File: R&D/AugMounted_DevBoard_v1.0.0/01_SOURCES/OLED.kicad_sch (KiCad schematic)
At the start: 30 parts, among them J3 J_FH43BW-61S-0.2SHW, Q1 Q_BSS123WQ-7-F, U4 U_TXB0108PWR, U5 U_TXB0108PWR, U6 U_TXB0108PWR

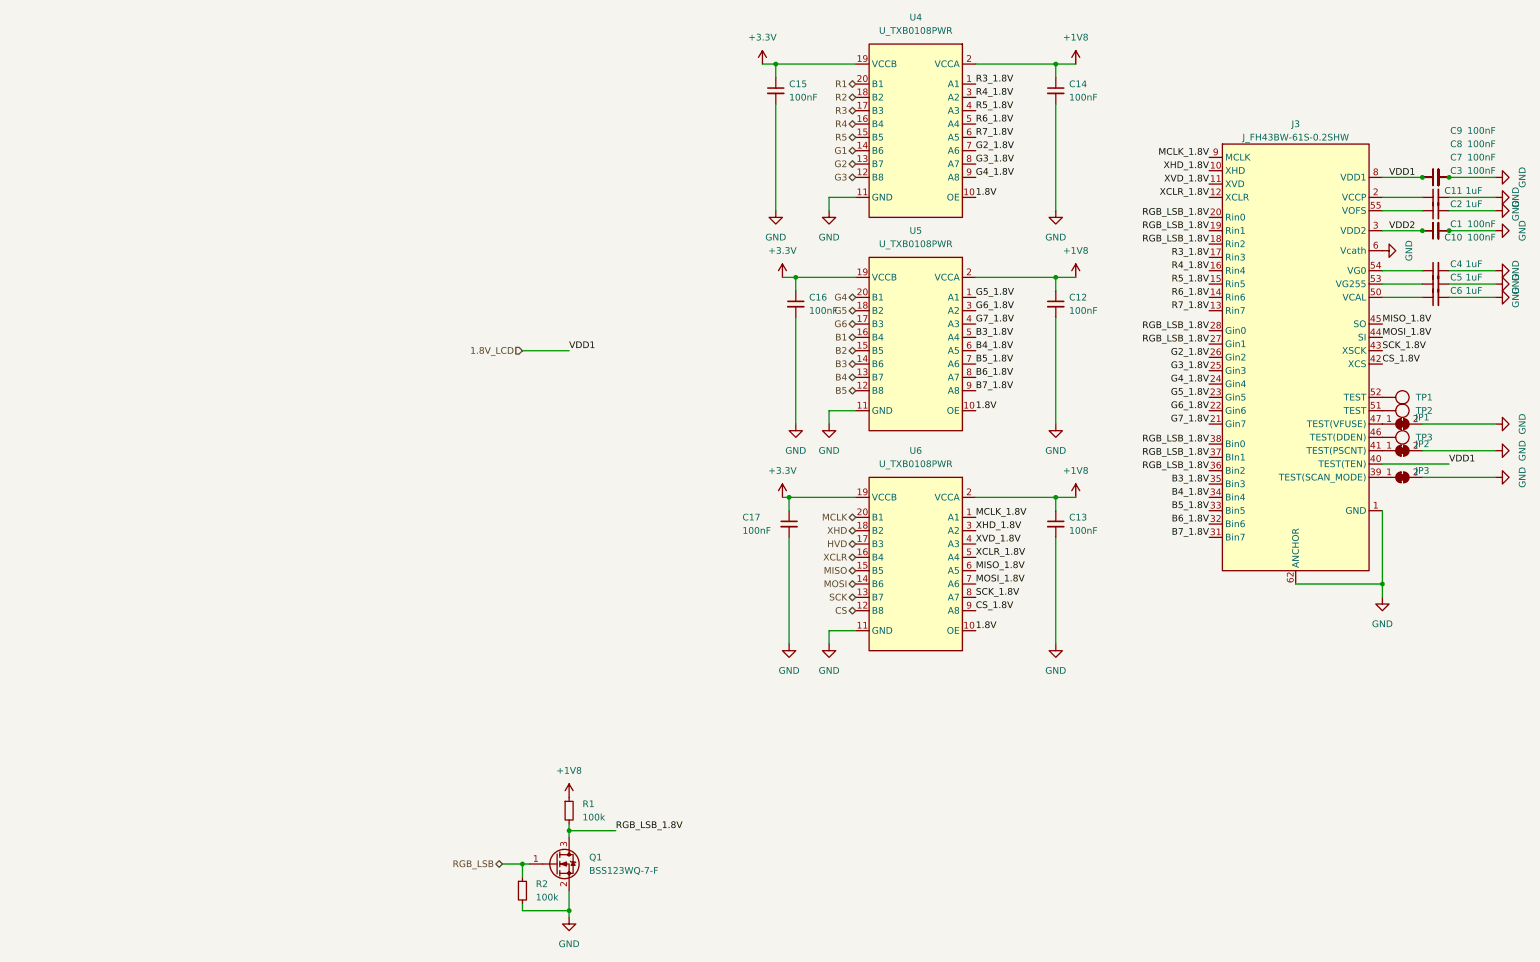
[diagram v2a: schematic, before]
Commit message: Schematic done
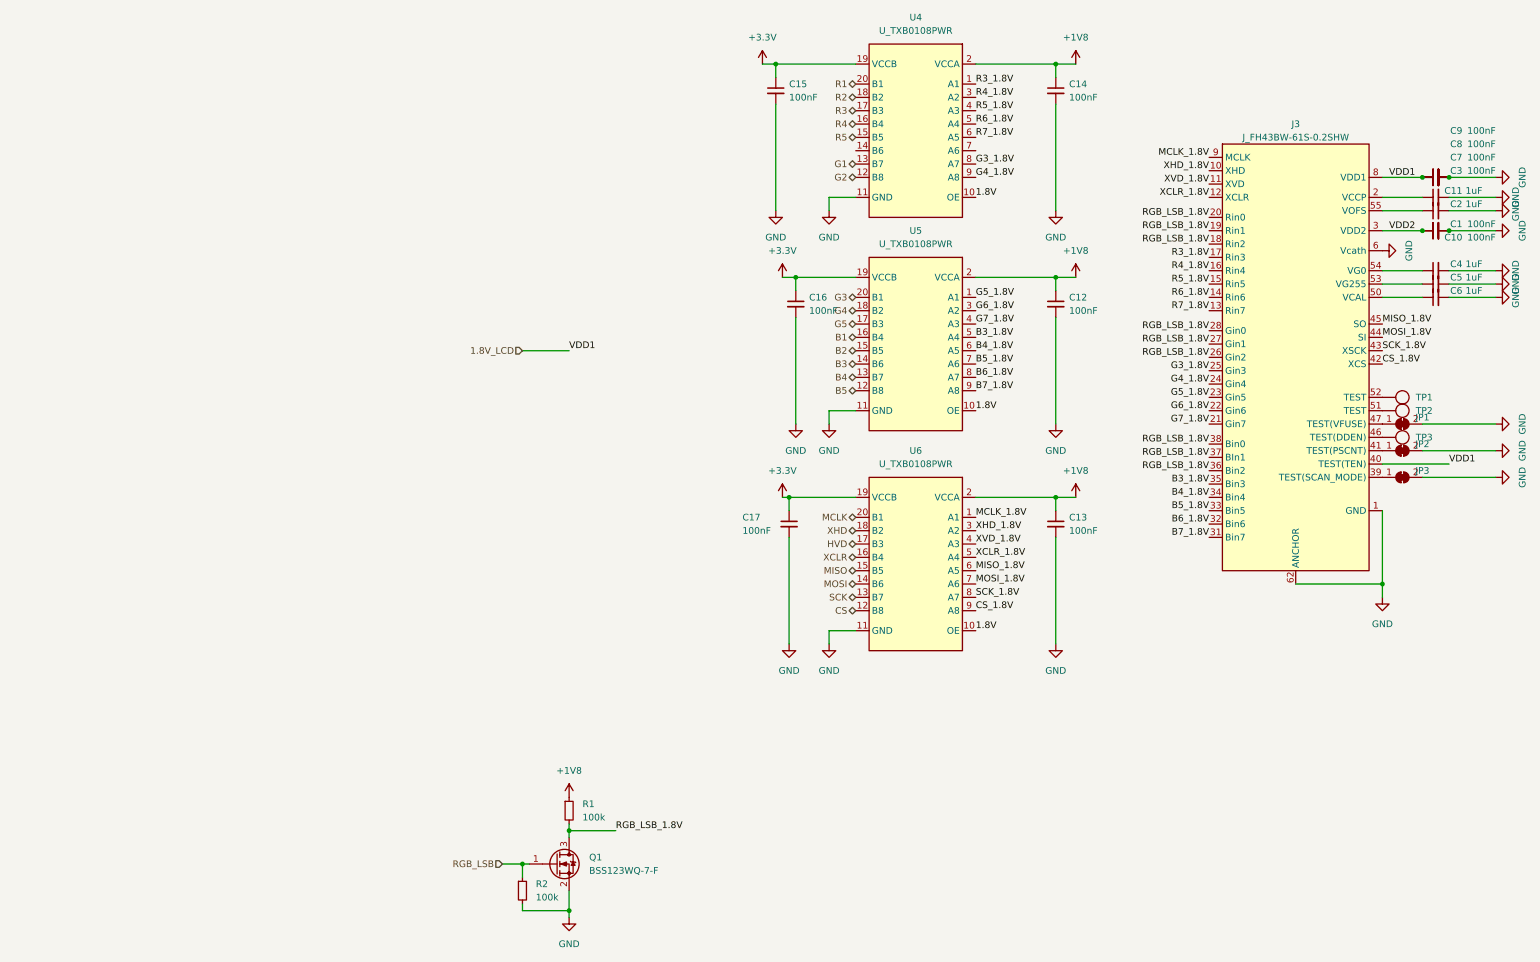
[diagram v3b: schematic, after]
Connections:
- net G6 is gone; now on net G5: U5.17 (B3)
- net G1: now also U4.13 (B7); no longer U4.14 (B6)
- net G2: now also U4.12 (B8); no longer U4.13 (B7)
- net G3: now also U5.20 (B1); no longer U4.12 (B8)
- net G4: now also U5.18 (B2); no longer U5.20 (B1)
- net G5: no longer U5.18 (B2)
- net RGB_LSB_1.8V: now also J3.26 (Gin2)
- net G2_1.8V: no longer names the net of U4.7 (A6)
- net G2_1.8V: no longer J3.26 (Gin2)
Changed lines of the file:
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@@
-    (effects (font (size 1.27 1.27)) (justify right bottom))
-  )
-  (label "G2_1.8V" (at 243.84 80.01 180) (fields_autoplaced)
     (effects (font (size 1.27 1.27)) (justify right bottom))
   )
@@
     (effects (font (size 1.27 1.27)) (justify right bottom))
   )
+  (label "RGB_LSB_1.8V" (at 243.84 80.01 180) (fields_autoplaced)
+    (effects (font (size 1.27 1.27)) (justify right bottom))
+  )
   (label "RGB_LSB_1.8V" (at 243.84 58.42 180) (fields_autoplaced)
     (effects (font (size 1.27 1.27)) (justify right bottom))
@@
     (effects (font (size 1.27 1.27)) (justify right bottom))
   )
-  (label "G2_1.8V" (at 199.39 40.64 0) (fields_autoplaced)
-    (effects (font (size 1.27 1.27)) (justify left bottom))
-  )
   (label "VDD2" (at 278.13 55.88 0) (fields_autoplaced)
     (effects (font (size 1.27 1.27)) (justify left bottom))
@@
     (effects (font (size 1.27 1.27)) (justify left bottom))
   )
-  (hierarchical_label "G2" (shape bidirectional) (at 176.53 43.18 180) (fields_autoplaced)
-    (effects (font (size 1.27 1.27)) (justify right))
-  )
   (hierarchical_label "XHD" (shape bidirectional) (at 176.53 113.03 180) (fields_autoplaced)
     (effects (font (size 1.27 1.27)) (justify right))
   )
+  (hierarchical_label "G2" (shape bidirectional) (at 176.53 45.72 180) (fields_autoplaced)
+    (effects (font (size 1.27 1.27)) (justify right))
+  )
   (hierarchical_label "B1" (shape bidirectional) (at 176.53 76.2 180) (fields_autoplaced)
     (effects (font (size 1.27 1.27)) (justify right))
   )
-  (hierarchical_label "G1" (shape bidirectional) (at 176.53 40.64 180) (fields_autoplaced)
-    (effects (font (size 1.27 1.27)) (justify right))
-  )
-  (hierarchical_label "G6" (shape bidirectional) (at 176.53 73.66 180) (fields_autoplaced)
+  (hierarchical_label "G3" (shape bidirectional) (at 176.53 68.58 180) (fields_autoplaced)
     (effects (font (size 1.27 1.27)) (justify right))
   )
@@
     (effects (font (size 1.27 1.27)) (justify right))
   )
-  (hierarchical_label "RGB_LSB" (shape bidirectional) (at 109.22 176.53 180) (fields_autoplaced)
+  (hierarchical_label "RGB_LSB" (shape input) (at 109.22 176.53 180) (fields_autoplaced)
     (effects (font (size 1.27 1.27)) (justify right))
   )
@@
     (effects (font (size 1.27 1.27)) (justify right))
   )
-  (hierarchical_label "G5" (shape bidirectional) (at 176.53 71.12 180) (fields_autoplaced)
+  (hierarchical_label "G1" (shape bidirectional) (at 176.53 43.18 180) (fields_autoplaced)
+    (effects (font (size 1.27 1.27)) (justify right))
+  )
+  (hierarchical_label "G5" (shape bidirectional) (at 176.53 73.66 180) (fields_autoplaced)
     (effects (font (size 1.27 1.27)) (justify right))
   )
@@
     (effects (font (size 1.27 1.27)) (justify right))
   )
-  (hierarchical_label "G3" (shape bidirectional) (at 176.53 45.72 180) (fields_autoplaced)
-    (effects (font (size 1.27 1.27)) (justify right))
-  )
-  (hierarchical_label "G4" (shape bidirectional) (at 176.53 68.58 180) (fields_autoplaced)
-    (effects (font (size 1.27 1.27)) (justify right))
-  )
+  (hierarchical_label "G4" (shape bidirectional) (at 176.53 71.12 180) (fields_autoplaced)
+    (effects (font (size 1.27 1.27)) (justify right))
+  )

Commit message: First revision of the layout
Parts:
- renumbered C15 to C401, C17 to C402, C16 to C403, C14 to C404, C12 to C405, C13 to C406, C3 to C407, C9 to C408, C8 to C409, C7 to C410, C11 to C411, C2 to C412, C1 to C413, C10 to C414, C4 to C415, C5 to C416, C6 to C417, J3 to J?, JP1 to JP401, JP2 to JP402, JP3 to JP403, Q1 to Q401, R2 to R401, R1 to R402, TP1 to TP401, TP2 to TP402, TP3 to TP403, U4 to U401, U5 to U402, U6 to U403

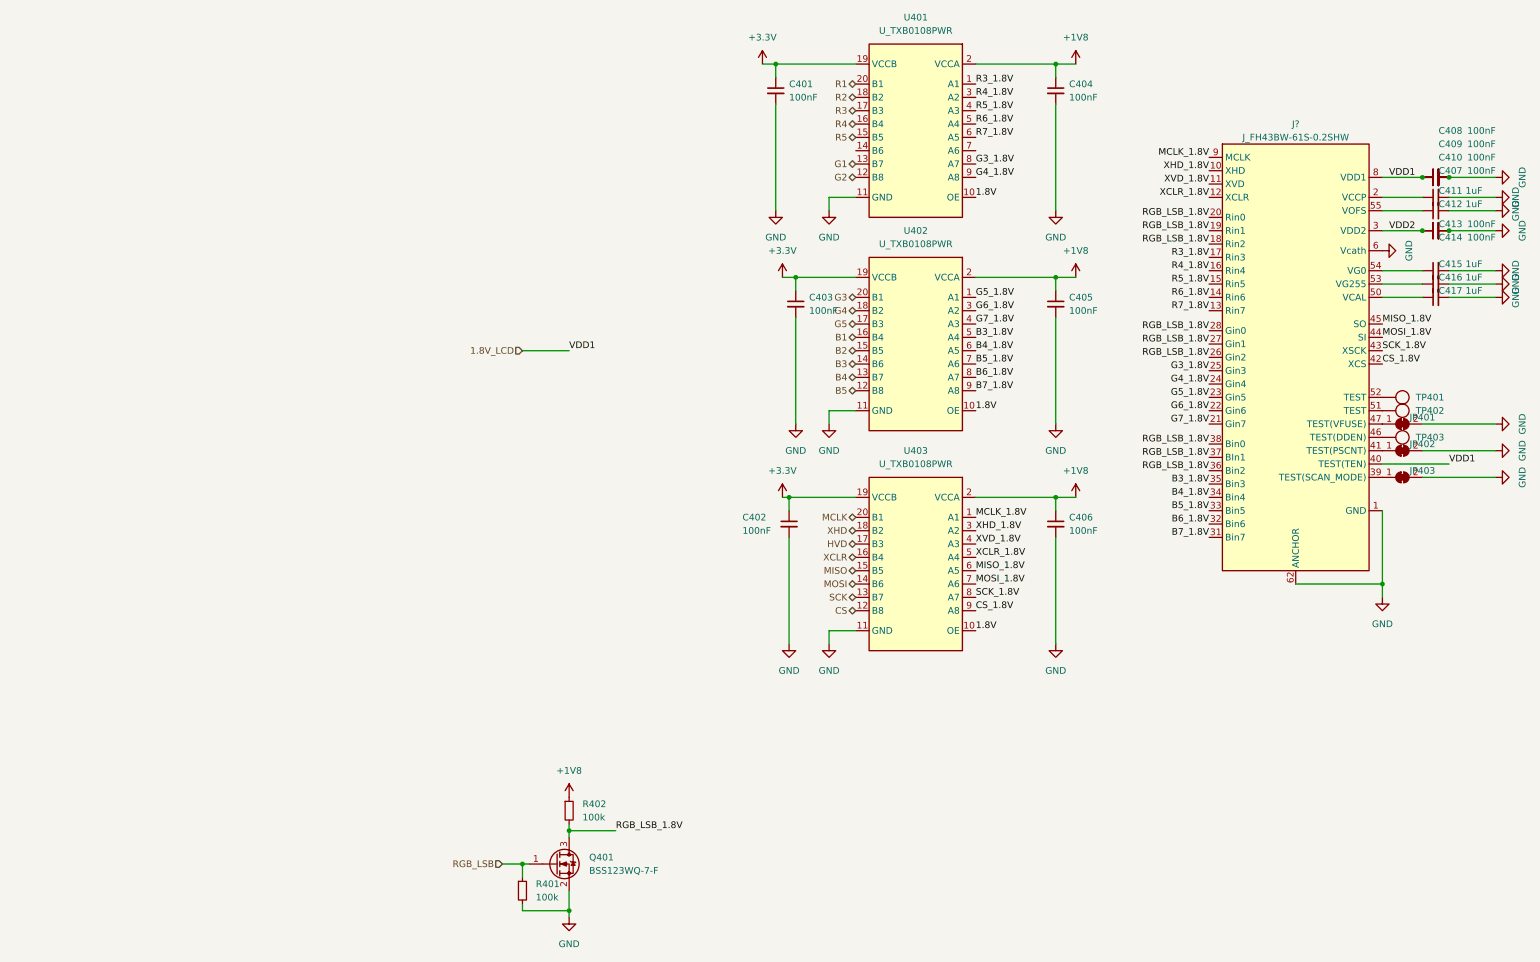
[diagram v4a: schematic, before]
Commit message: Changed layout + all passive to 0402
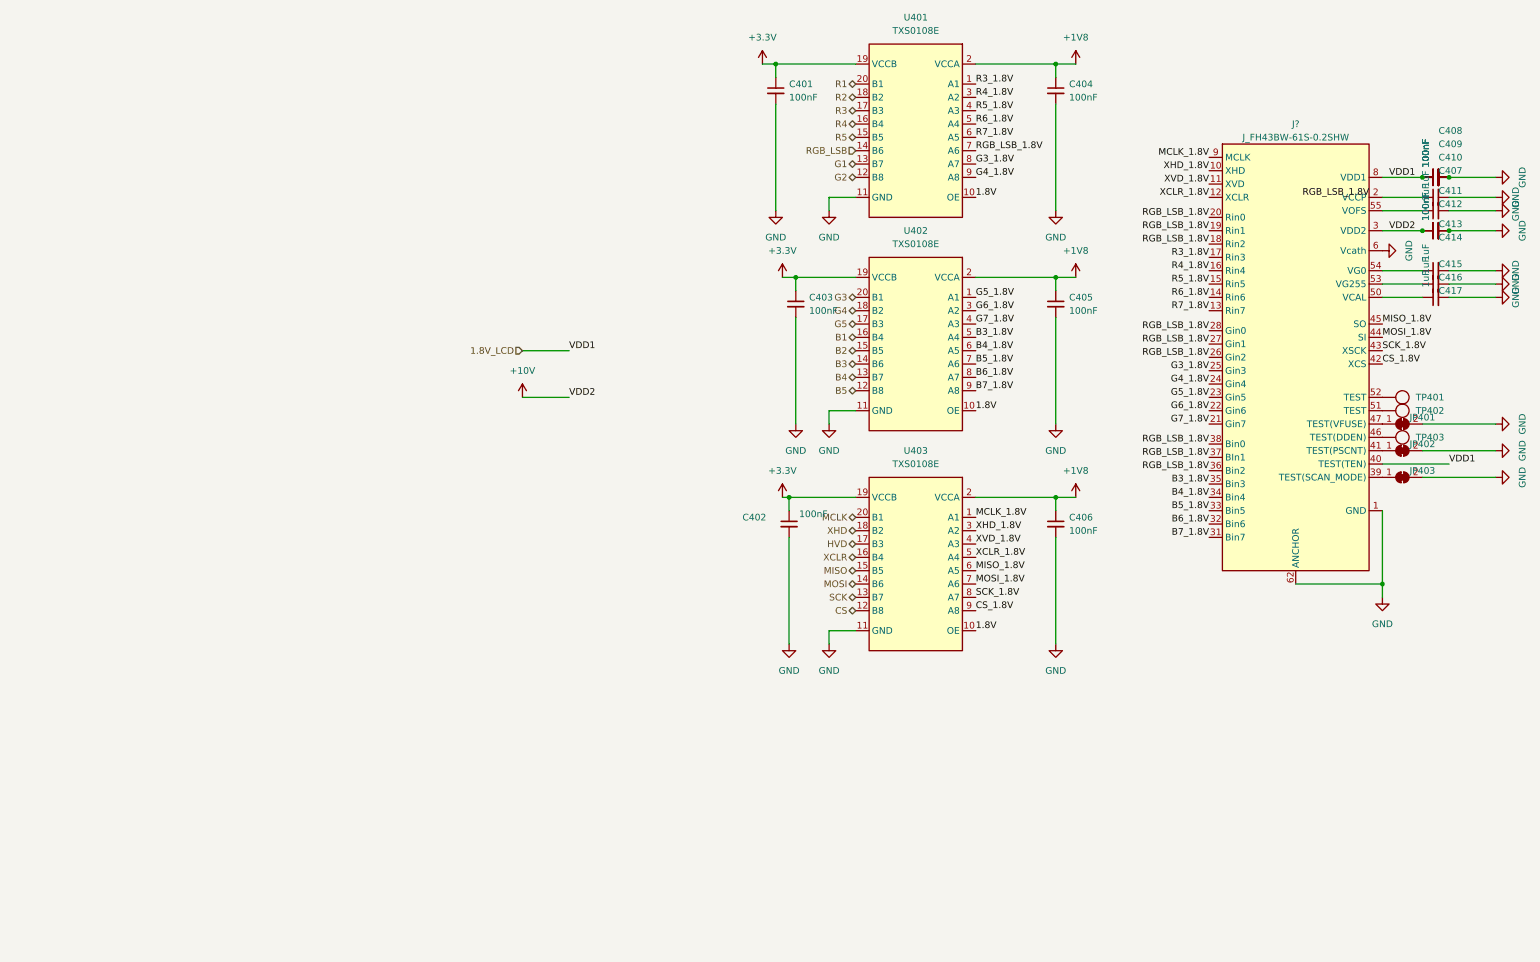
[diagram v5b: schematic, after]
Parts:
- removed Q401: Q_BSS123WQ-7-F, .mounted-lib:SOT-323_SC-70_DIODES_INC, symbol .mounted-lib:Q_BSS123WQ-7-F
- removed R401, R402: R_0603_100k_1%_0.1W, .mounted-lib:R_0603_1608Metric, symbol .mounted-lib:R_0603_100k_1%_0.1W
- removed U401, U402, U403: U_TXB0108PWR, .mounted-lib:TSSOP-20_4.4x6.5mm_P0.65mm_TEXAS_INSTRUMENTS, symbol .mounted-lib:U_TXB0108PWR
- added U401, U402, U403: U_TXS0108E, .mounted-lib:VQFN-20_TEXAS_INSTRUMENTS, symbol .mounted-lib:U_TXS0108E
- C401, C402, C403, C404, C405, C406, C407, C408, C409, C410, C413, C414: footprint .mounted-lib:C_0603_1608Metric -> .mounted-lib:C_0402_1005Metric; symbol .mounted-lib:C_0603_100nF_100V_X7R_10% -> .mounted-lib:C_0402_100nF_50V_X7R_10%; CMP_ID 11 -> 1062; MaxHeight_mm 0.8mm -> 0.5mm; Voltage 100V -> 50V
- C411, C412, C415, C416, C417: value C_0805_1uF_100V_X7S_20% -> C_0402_1uF_10V_X7R_10%; footprint .mounted-lib:C_0805_1608Metric -> .mounted-lib:C_0402_1005Metric; symbol .mounted-lib:C_0805_1uF_100V_X7S_20% -> .mounted-lib:C_0402_1uF_10V_X7R_10%; CMP_ID 7 -> 1069; MaxHeight_mm 1.25mm -> 0.5mm; Package C0805 -> C0402; Tolerance 20% -> 10%; Voltage 100V -> 10V; _Created CCN 2022-05-12 -> JCN 2023-11-12
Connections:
- net +1V8: now also U401.2 (VCCA), U402.2 (VCCA), U403.2 (VCCA)
- net +3.3V: now also U401.19 (VCCB), U402.19 (VCCB), U403.19 (VCCB)
- net 1.8V: now also U401.10 (OE), U402.10 (OE), U403.10 (OE)
- net B1: now also U402.16 (B4)
- net B2: now also U402.15 (B5)
- net B3: now also U402.14 (B6)
- net B3_1.8V: now also U402.5 (A4)
- net B4: now also U402.13 (B7)
- net B4_1.8V: now also U402.6 (A5)
- net B5: now also U402.12 (B8)
- net B5_1.8V: now also U402.7 (A6)
- net B6_1.8V: now also U402.8 (A7)
- net B7_1.8V: now also U402.9 (A8)
- net CS: now also U403.12 (B8)
- net CS_1.8V: now also U403.9 (A8)
- net G1: now also U401.13 (B7)
- net G2: now also U401.12 (B8)
- net G3: now also U402.20 (B1)
- net G3_1.8V: now also U401.8 (A7)
- net G4: now also U402.18 (B2)
- net G4_1.8V: now also U401.9 (A8)
- net G5: now also U402.17 (B3)
- net G5_1.8V: now also U402.1 (A1)
- net G6_1.8V: now also U402.3 (A2)
- net G7_1.8V: now also U402.4 (A3)
- net GND: now also U401.11 (GND), U402.11 (GND), U403.11 (GND)
- net HVD: now also U403.17 (B3)
- net MCLK: now also U403.20 (B1)
- net MCLK_1.8V: now also U403.1 (A1)
- net MISO: now also U403.15 (B5)
- net MISO_1.8V: now also U403.6 (A5)
- net MOSI: now also U403.14 (B6)
- net MOSI_1.8V: now also U403.7 (A6)
- net R1: now also U401.20 (B1)
- net R2: now also U401.18 (B2)
- net R3: now also U401.17 (B3)
- net R3_1.8V: now also U401.1 (A1)
- net R4: now also U401.16 (B4)
- net R4_1.8V: now also U401.3 (A2)
- net R5: now also U401.15 (B5)
- net R5_1.8V: now also U401.4 (A3)
- net R6_1.8V: now also U401.5 (A4)
- net R7_1.8V: now also U401.6 (A5)
- net RGB_LSB: now also U401.14 (B6)
- net RGB_LSB_1.8V: now also U401.7 (A6)
- net SCK: now also U403.13 (B7)
- net SCK_1.8V: now also U403.8 (A7)
- net XCLR: now also U403.16 (B4)
- net XCLR_1.8V: now also U403.5 (A4)
- net XHD: now also U403.18 (B2)
- net XHD_1.8V: now also U403.3 (A2)
- net XVD_1.8V: now also U403.4 (A3)
- net VDD2 renamed +10V
